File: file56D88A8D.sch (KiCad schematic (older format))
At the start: 1 part

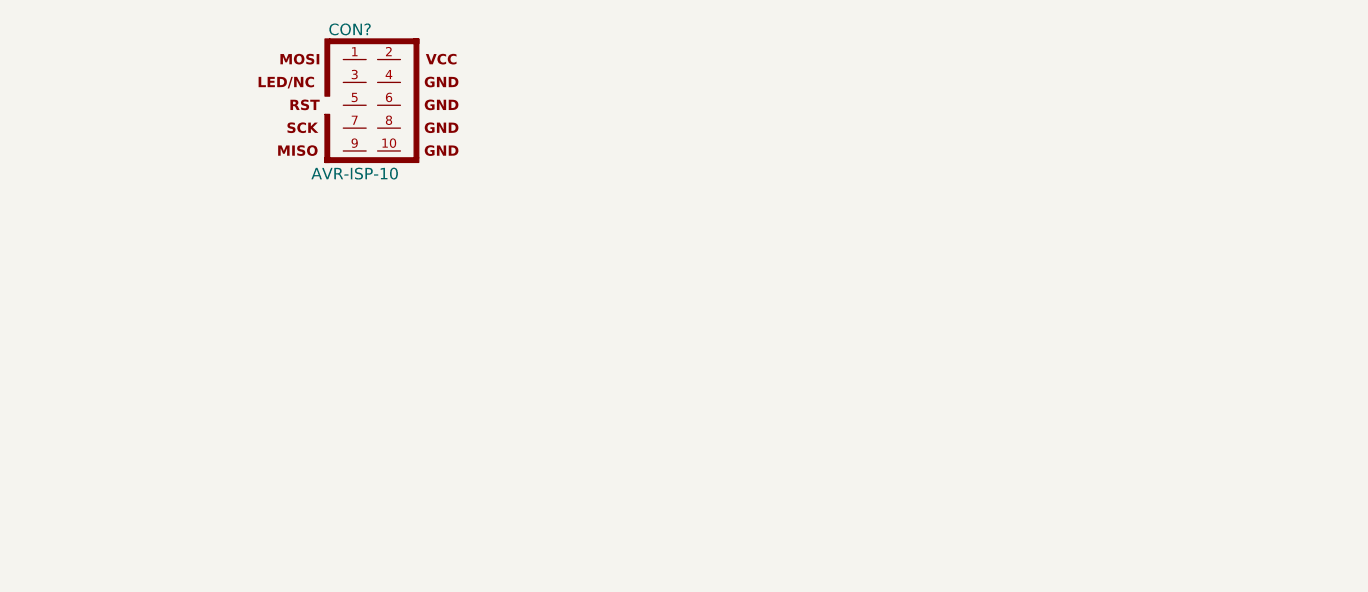
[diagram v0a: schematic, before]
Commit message: Подключены программатор, питание и генератор
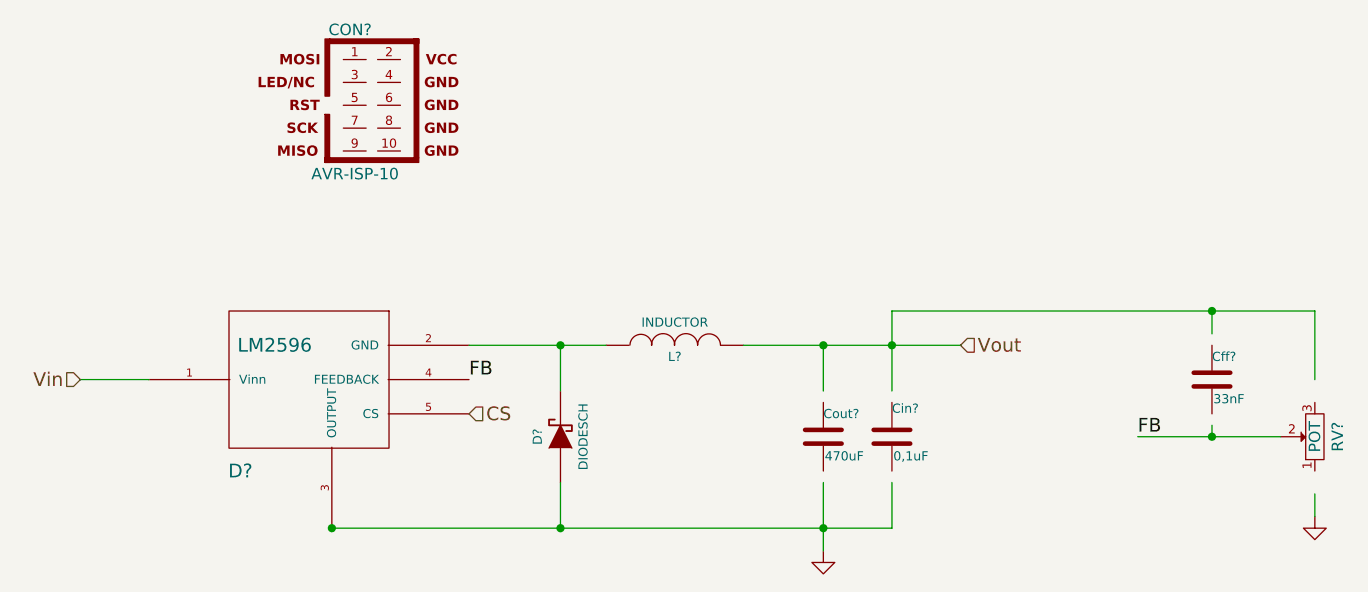
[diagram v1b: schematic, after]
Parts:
- added Cff?: 33nF, ~, symbol C
- added Cin?: 0,1uF, ~, symbol C
- added Cout?: 470uF, ~, symbol C
- added D?: DIODESCH, ~, symbol DIODESCH
- added D?: LM2596, ~, symbol LM2596
- added L?: INDUCTOR, ~, symbol INDUCTOR
- added RV?: POT, ~, symbol POT
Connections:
- net labels added: CS, FB, GND, Vin, Vout
- wire segments 0 -> 16
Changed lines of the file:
@@
 EESchema Schematic File Version 2
+LIBS:lm2596
 LIBS:power
 LIBS:device
@@
 LIBS:contrib
 LIBS:valves
+LIBS:LM2596-cache
 EELAYER 27 0
 EELAYER END
 $Descr A4 11693 8268
 encoding utf-8
-Sheet 1 1
+Sheet 2 2
 Title ""
-Date "4 mar 2016"
+Date "8 mar 2016"
 Rev ""
 Comp ""
@@
 	1    0    0    -1
 $EndComp
+$Comp
+L C Cin?
+U 1 1 56DED62E
+P 6350 3700
+F 0 "Cin?" H 6350 3800 40  0000 L BNN
+F 1 "0,1uF" H 6356 3615 40  0000 L CNN
+F 2 "~" V 6388 3550 30  0000 C CNN
+F 3 "~" H 6350 3700 60  0000 C CNN
+	1    6350 3700
+	1    0    0    -1
+$EndComp
+$Comp
+L C Cff?
+U 1 1 56DED634
+P 7750 3450
+F 0 "Cff?" H 7750 3550 40  0000 L CNN
+F 1 "33nF" H 7756 3365 40  0000 L CNN
+F 2 "~" H 7788 3300 30  0000 C CNN
+F 3 "~" H 7750 3450 60  0000 C CNN
+	1    7750 3450
+	1    0    0    -1
+$EndComp
+$Comp
+L DIODESCH D?
+U 1 1 56DED63A
+P 4900 3700
+F 0 "D?" H 4900 3800 40  0000 C CNN
+F 1 "DIODESCH" H 4900 3600 40  0000 C CNN
+F 2 "~" H 4900 3700 60  0000 C CNN
+F 3 "~" H 4900 3700 60  0000 C CNN
+	1    4900 3700
+	0    -1   -1   0
+$EndComp
+$Comp
+L INDUCTOR L?
+U 1 1 56DED640
+P 5400 3300
+F 0 "L?" V 5350 3300 40  0000 C CNN
+F 1 "INDUCTOR" V 5500 3300 40  0000 C CNN
+F 2 "~" H 5400 3300 60  0000 C CNN
+F 3 "~" H 5400 3300 60  0000 C CNN
+	1    5400 3300
+	0    -1   -1   0
+$EndComp
+$Comp
+L C Cout?
+U 1 1 56DED646
+P 6050 3700
+F 0 "Cout?" H 6050 3800 40  0000 L CNN
+F 1 "470uF" H 6056 3615 40  0000 L CNN
+F 2 "~" H 6088 3550 30  0000 C CNN
+F 3 "~" H 6050 3700 60  0000 C CNN
+	1    6050 3700
+	1    0    0    -1
+$EndComp
+Wire Wire Line
+	4500 3300 5100 3300
+Wire Wire Line
+	5700 3300 6650 3300
+Wire Wire Line
+	6050 3300 6050 3500
+Wire Wire Line
+	6350 3150 6350 3500
+Connection ~ 6050 3300
+Wire Wire Line
+	7750 3250 7750 3150
+Wire Wire Line
+	6350 3150 8200 3150
+Connection ~ 6350 3300
+Wire Wire Line
+	8200 3150 8200 3450
+Connection ~ 7750 3150
+Wire Wire Line
+	7425 3700 8050 3700
+Wire Wire Line
+	7750 3700 7750 3650
+Connection ~ 7750 3700
+Wire Wire Line
+	4900 4100 4900 3900
+Connection ~ 3900 4100
+Wire Wire Line
+	4900 3500 4900 3300
+Connection ~ 4900 3300
+Wire Wire Line
+	6050 3900 6050 4200
+Connection ~ 4900 4100
+Wire Wire Line
+	6350 4100 6350 3900
+Connection ~ 6050 4100
+Wire Wire Line
+	2800 3450 3100 3450
+Text HLabel 2800 3450 0    60   Input ~ 0
+Vin
+Text Label 4500 3450 0    60   ~ 0
+FB
+Text Label 7425 3700 0    60   ~ 0
+FB
+Text HLabel 6650 3300 2    60   Input ~ 0
+Vout
+$Comp
+L GND #PWR?
+U 1 1 56DED666
+P 6050 4200
+F 0 "#PWR?" H 6050 4200 30  0001 C CNN
+F 1 "GND" H 6050 4130 30  0001 C CNN
+F 2 "" H 6050 4200 60  0000 C CNN
+F 3 "" H 6050 4200 60  0000 C CNN
+	1    6050 4200
+	1    0    0    -1
+$EndComp
+$Comp
+L GND #PWR?
+U 1 1 56DED66C
+P 8200 4050
+F 0 "#PWR?" H 8200 4050 30  0001 C CNN
+F 1 "GND" H 8200 3980 30  0001 C CNN
+F 2 "" H 8200 4050 60  0000 C CNN
+F 3 "" H 8200 4050 60  0000 C CNN
+	1    8200 4050
+	1    0    0    -1
+$EndComp
+Wire Wire Line
+	8200 3950 8200 4050
+Text HLabel 4500 3600 2    60   Input ~ 0
+CS
+$Comp
+L POT RV?
+U 1 1 56DED674
+P 8200 3700
+F 0 "RV?" H 8200 3600 50  0000 C CNN
+F 1 "POT" H 8200 3700 50  0000 C CNN
+F 2 "~" H 8200 3700 60  0000 C CNN
+F 3 "~" H 8200 3700 60  0000 C CNN
+	1    8200 3700
+	0    -1   -1   0
+$EndComp
+$Comp
+L LM2596 D?
+U 1 1 56DED67A
+P 3450 3100
+F 0 "D?" H 3500 2350 60  0000 C CNN
+F 1 "LM2596" H 3650 2900 60  0000 C CNN
+F 2 "~" H 3450 3100 60  0000 C CNN
+F 3 "~" H 3450 3100 60  0000 C CNN
+	1    3450 3100
+	1    0    0    -1
+$EndComp
+Wire Wire Line
+	3900 4100 6350 4100
 $EndSCHEMATC
